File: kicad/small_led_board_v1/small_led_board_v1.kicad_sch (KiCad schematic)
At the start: 107 parts, among them J1 TO FPGA, J2 +5V IN, Q1 IRLZ44N, Q10 IRF4905, Q11 IRF4905, Q12 IRF4905, Q13 IRF4905, Q14 IRF4905, Q15 IRLZ44N, Q16 IRLZ44N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

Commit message: kicad: renamed project to v1
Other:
- title: Small LED Board -> Small LED Board v1
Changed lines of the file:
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@@
 	(paper "A4")
 	(title_block
-		(title "Small LED Board")
-		(rev "1.0")
+		(title "Small LED Board v1")
 	)
 	(junction

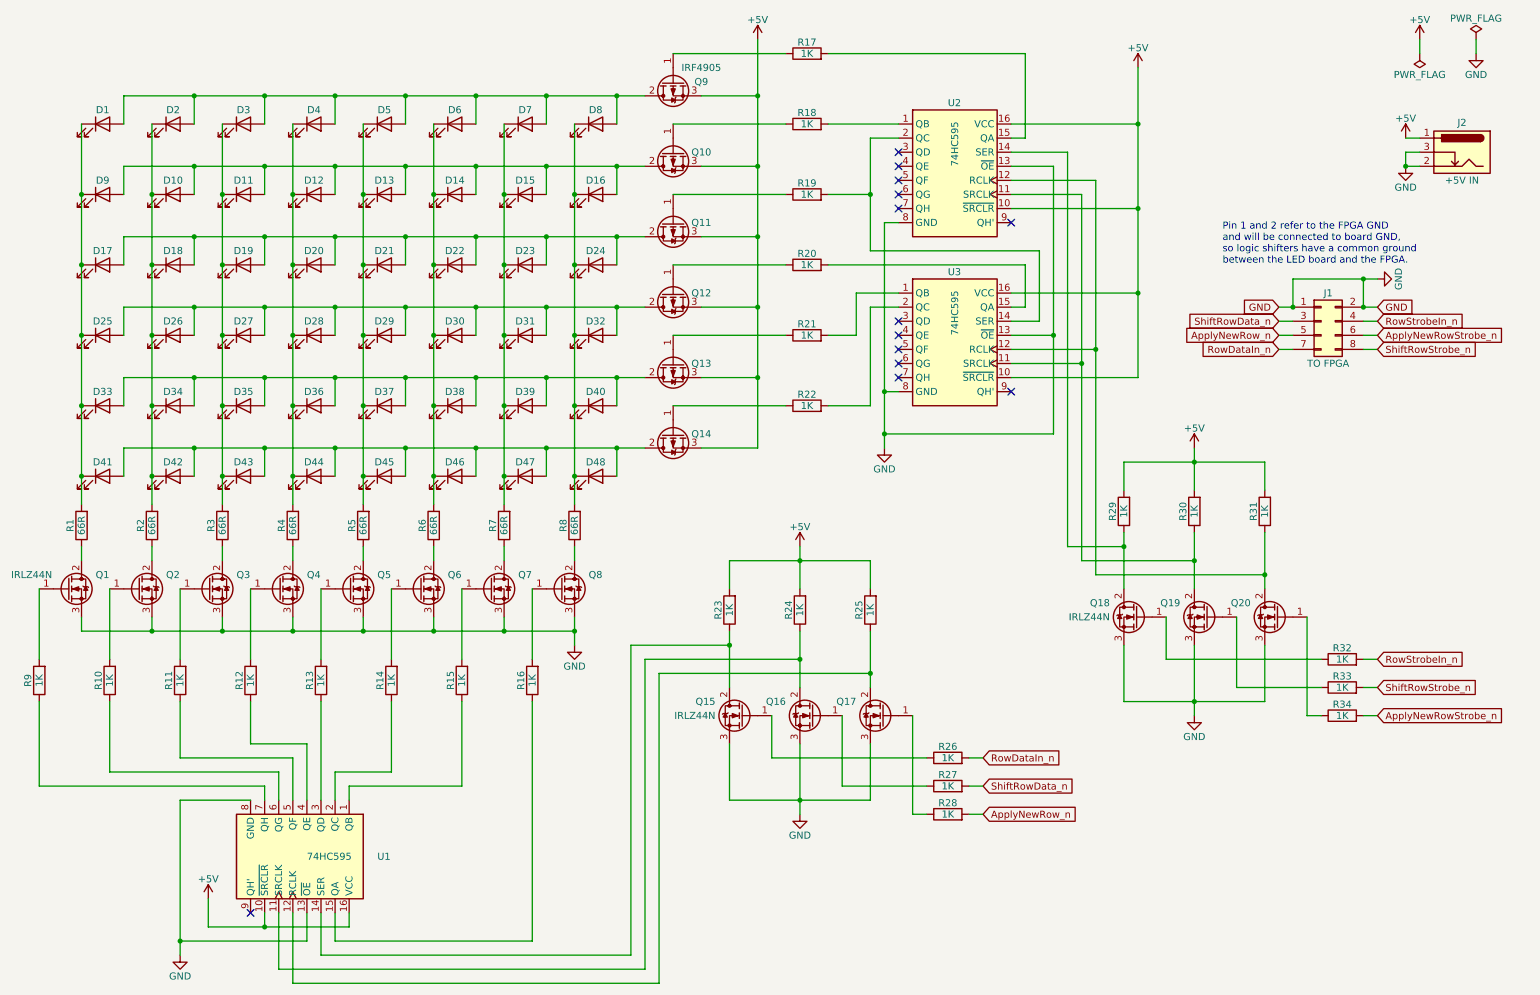
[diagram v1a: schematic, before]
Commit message: kicad: migration complete to 9.0, small led boards both done
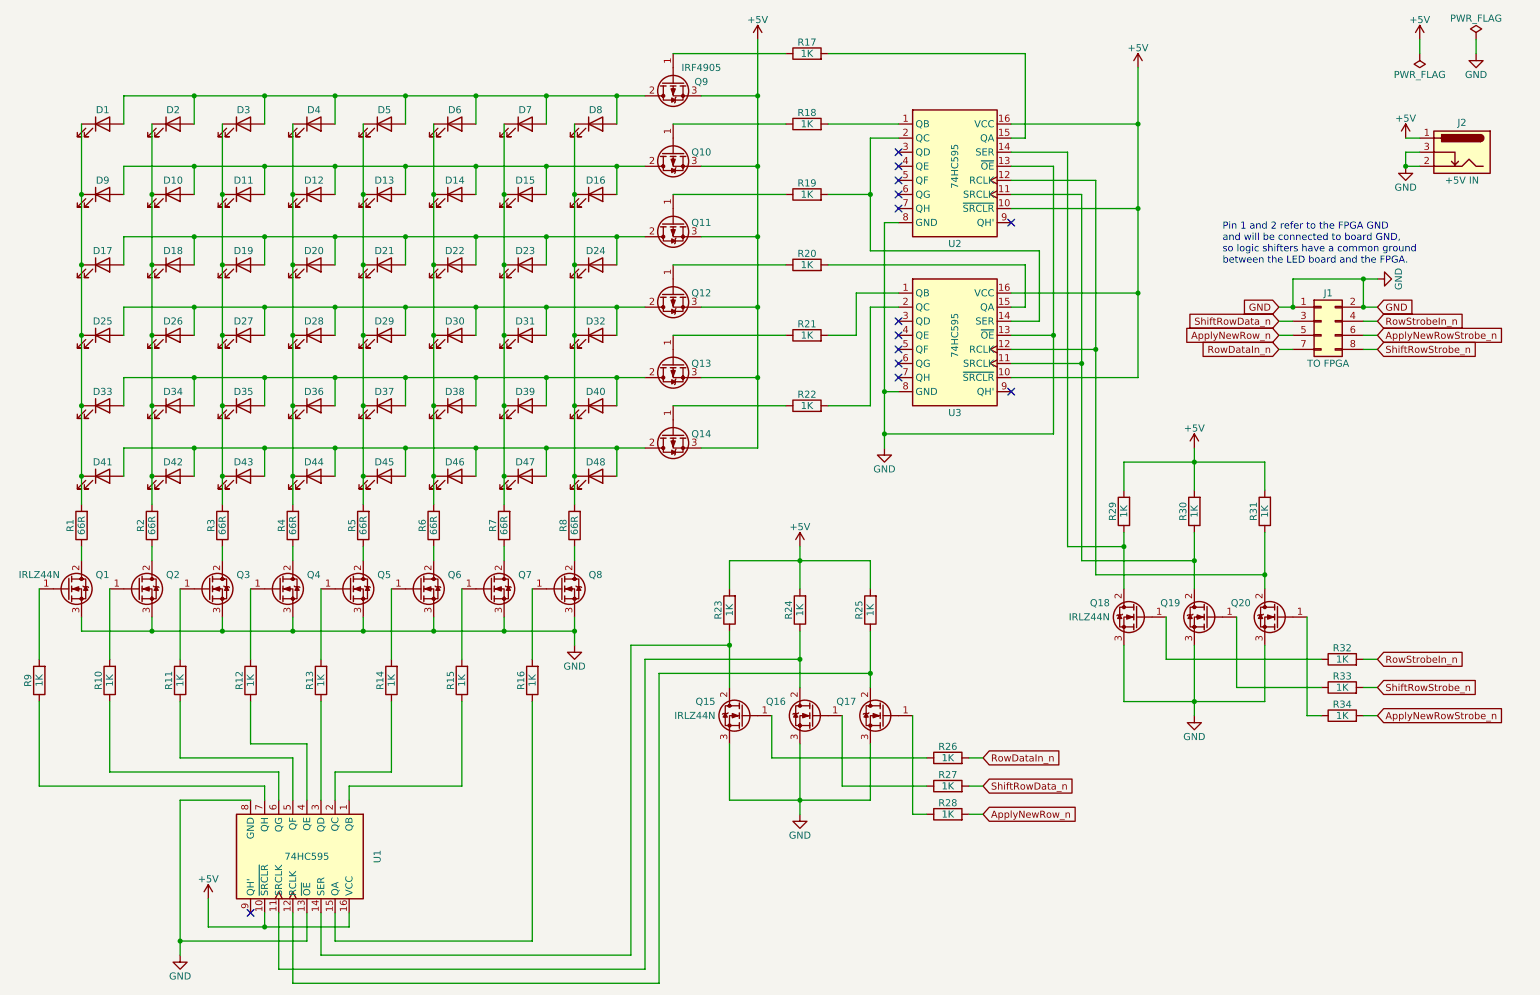
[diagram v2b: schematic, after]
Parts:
- removed U1, U2, U3: 74HC595, Package_DIP:DIP-16_W7.62mm, symbol 74xx:74HC595
- added U1, U2, U3: 74HC595, Package_DIP:DIP-16_W7.62mm, symbol symbol_library:74HC595
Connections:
- net +5V: now also U1.10 (~{SRCLR}), U1.16 (VCC), U2.10 (~{SRCLR}), U2.16 (VCC), U3.10 (~{SRCLR}), U3.16 (VCC)
- net GND: now also U1.13 (~{OE}), U1.8 (GND), U2.13 (~{OE}), U2.8 (GND), U3.13 (~{OE}), U3.8 (GND)
- net at Q18.2 (D), R29.1: now also U2.14 (SER)
- net at R18.2: now also U2.1 (QB)
- net at Q17.2 (D), R25.1: now also U1.12 (RCLK)
- net at Q16.2 (D), R24.1: now also U1.11 (SRCLK)
- net at R19.2: now also U2.2 (QC), U3.14 (SER)
- net at Q15.2 (D), R23.1: now also U1.14 (SER)
- net at R12.1: now also U1.4 (QE)
- net at R16.1: now also U1.15 (QA)
- net at R14.1: now also U1.2 (QC)
- net at R17.2: now also U2.15 (QA)
- net at R20.2: now also U3.15 (QA)
- net at Q19.2 (D), R30.1: now also U2.11 (SRCLK), U3.11 (SRCLK)
- net at R11.1: now also U1.5 (QF)
- net at R15.1: now also U1.1 (QB)
- net at R13.1: now also U1.3 (QD)
- net at R10.1: now also U1.6 (QG)
- net at R9.1: now also U1.7 (QH)
- net at R21.2: now also U3.1 (QB)
- net at R22.2: now also U3.2 (QC)
- net at Q20.2 (D), R31.1: now also U2.12 (RCLK), U3.12 (RCLK)
